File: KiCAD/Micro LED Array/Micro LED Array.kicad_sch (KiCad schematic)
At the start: 17 parts, among them J1 JST-XH

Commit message: revise border
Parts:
- removed D15, D16: LED, Custom footprints:LED_XLAMP_XE-G_CRW, symbol Device:LED
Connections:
- net GND: now also D14.1 (K)
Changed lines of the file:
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@@
-    )
-  )
-  (symbol (lib_id "Device:LED") (at 107.95 91.44 0) (mirror x) (unit 1)
-    (in_bom yes) (on_board yes) (dnp no) (fields_autoplaced)
-    (property "Reference" "D15" (at 106.3625 86.2711 0)
-      (effects (font (size 1.27 1.27)))
-    )
-    (property "Value" "LED" (at 106.3625 88.1921 0)
-      (effects (font (size 1.27 1.27)))
-    )
-    (property "Footprint" "Custom footprints:LED_XLAMP_XE-G_CRW" (at 107.95 91.44 0)
-      (effects (font (size 1.27 1.27)) hide)
-    )
-    (property "Datasheet" "https://downloads.cree-led.com/files/ds/x/XLamp-XE-G.pdf" (at 107.95 91.44 0)
-      (effects (font (size 1.27 1.27)) hide)
-    )
-    (property "Manufacturer" "Cree LED" (at 107.95 91.44 0)
-      (effects (font (size 1.27 1.27)) hide)
-    )
-    (property "Part" "XEGARY-H0-0000-000-000000K2001" (at 107.95 91.44 0)
-      (effects (font (size 1.27 1.27)) hide)
-    )
-    (pin "1")
-    (pin "2")
-    (instances
-      (project "Micro LED Array"
-        (path "/501b6f31-167f-4148-be11-c5bed0bfbf7d"
-          (reference "D15") (unit 1)
-        )
-      )
     )
   )
@@
     )
   )
-  (symbol (lib_id "power:GND") (at 96.52 91.44 0) (unit 1)
+  (symbol (lib_id "power:GND") (at 111.76 91.44 0) (unit 1)
     (in_bom yes) (on_board yes) (dnp no)
-    (property "Reference" "#PWR02" (at 96.52 97.79 0)
+    (property "Reference" "#PWR02" (at 111.76 97.79 0)
       (effects (font (size 1.27 1.27)) hide)
     )
-    (property "Value" "GND" (at 97.79 95.25 0)
+    (property "Value" "GND" (at 113.03 95.25 0)
       (effects (font (size 1.27 1.27)))
     )
-    (property "Footprint" "" (at 96.52 91.44 0)
+    (property "Footprint" "" (at 111.76 91.44 0)
       (effects (font (size 1.27 1.27)) hide)
     )
-    (property "Datasheet" "" (at 96.52 91.44 0)
+    (property "Datasheet" "" (at 111.76 91.44 0)
       (effects (font (size 1.27 1.27)) hide)
     )
@@
         )
       )
-    )
-  )
-  (symbol (lib_id "Device:LED") (at 100.33 91.44 0) (mirror x) (unit 1)
-    (in_bom yes) (on_board yes) (dnp no) (fields_autoplaced)
-    (property "Reference" "D16" (at 98.7425 86.2711 0)
-      (effects (font (size 1.27 1.27)))
-    )
-    (property "Value" "LED" (at 98.7425 88.1921 0)
-      (effects (font (size 1.27 1.27)))
-    )
-    (property "Footprint" "Custom footprints:LED_XLAMP_XE-G_CRW" (at 100.33 91.44 0)
-      (effects (font (size 1.27 1.27)) hide)
-    )
-    (property "Datasheet" "https://downloads.cree-led.com/files/ds/x/XLamp-XE-G.pdf" (at 100.33 91.44 0)
-      (effects (font (size 1.27 1.27)) hide)
-    )
-    (property "Manufacturer" "Cree LED" (at 100.33 91.44 0)
-      (effects (font (size 1.27 1.27)) hide)
-    )
-    (property "Part" "XEGARY-H0-0000-000-000000K2001" (at 100.33 91.44 0)
-      (effects (font (size 1.27 1.27)) hide)
-    )
-    (pin "1")
-    (pin "2")
-    (instances
-      (project "Micro LED Array"
-        (path "/501b6f31-167f-4148-be11-c5bed0bfbf7d"
-          (reference "D16") (unit 1)
-        )
-      )

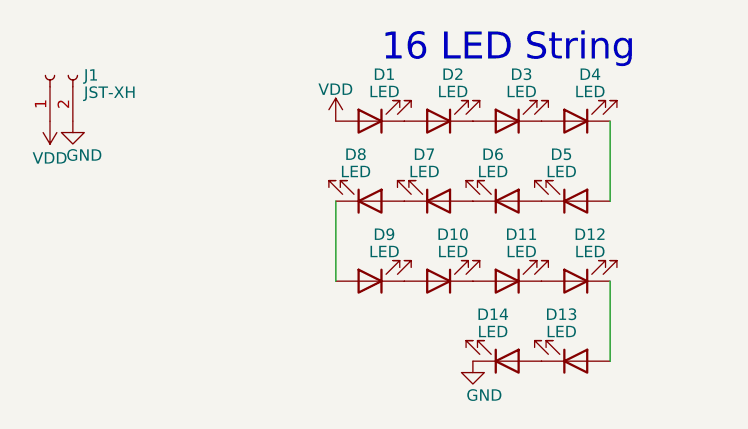
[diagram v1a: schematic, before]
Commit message: Widen wire spacing
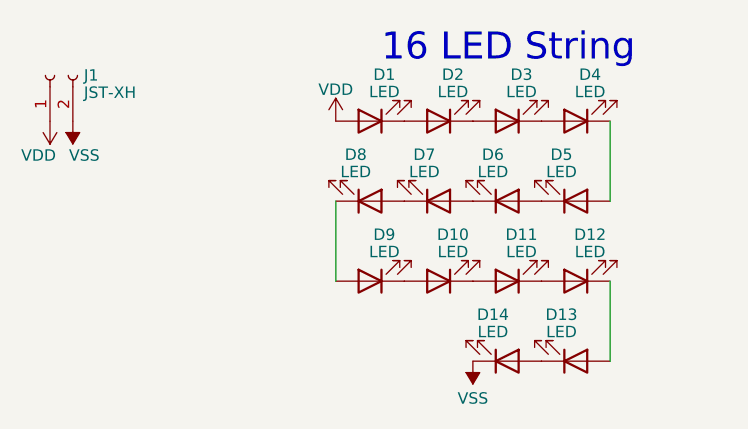
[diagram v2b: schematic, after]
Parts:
- J1: footprint Connector_Wire:SolderWire-0.1sqmm_1x02_P3.6mm_D0.4mm_OD1mm -> Custom footprints:SolderWire-0.1sqmm_1x02_P9.6mm_D0.4mm_OD1mm
- renumbered D14 to D13, D13 to D14, D8 to D5, D7 to D6, D6 to D7, D5 to D8
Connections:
- net at D13.2 (A): now also D12.1 (K); no longer D14.1 (K)
- net at D8.1 (K): now also D9.2 (A); no longer D7.2 (A)
- net at D8.2 (A): now also D7.1 (K); no longer D4.1 (K)
- net at D6.2 (A): now also D5.1 (K); no longer D7.1 (K)
- net at D14.2 (A): now also D13.1 (K); no longer D12.1 (K)
- net at D6.1 (K): now also D7.2 (A); no longer D5.2 (A)
- net GND renamed VSS
- net VSS: now also D14.1 (K); no longer D13.1 (K)
- new net: D4.1 (K), D5.2 (A)
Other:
- moved on the sheet: D13, D14, D5, D6, D7, D8

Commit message: Ordered version
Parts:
- J1: footprint Custom footprints:SolderWire-0.1sqmm_1x02_P9.6mm_D0.4mm_OD1mm -> Custom footprints:SolderWire-0.5sqmm_1x02_P10.5mm_D0.9mm_OD2.1mm
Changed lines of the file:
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@@
       (effects (font (size 1.27 1.27)) (justify right))
     )
-    (property "Footprint" "Custom footprints:SolderWire-0.1sqmm_1x02_P9.6mm_D0.4mm_OD1mm" (at 64.77 59.69 0)
+    (property "Footprint" "Custom footprints:SolderWire-0.5sqmm_1x02_P10.5mm_D0.9mm_OD2.1mm" (at 64.77 59.69 0)
       (effects (font (size 1.27 1.27)) hide)
     )
